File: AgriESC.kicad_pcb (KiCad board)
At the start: 2 copper layers, 80.8 x 69.6 mm, 309 parts, among them J1 SUPPLY, J10 GPIO, J11 USB_OTG, J12 HALL_ENC, J2 PH_A, J3 PH_B, J4 PH_C, J6 COMM, J7 SERVO, J8 CAN, J9 SWD, SW1 SW_SPDT, U1 FDMS7698, U10 STM32F405RGT6, U11 DRV8303, U12 TJA1051TK-3, U13 LMR16006YQ, U14 MCP1700-3302E_SOT23, U15 MCP1700-3302E_SOT23, U2 FDMS7698, U3 FDMS7698, U4 FDMS7698, U5 FDMS7698, U6 FDMS7698, U7 MAX9920, U8 MAX9920, U9 MAX9920, Y1 8M Resonator

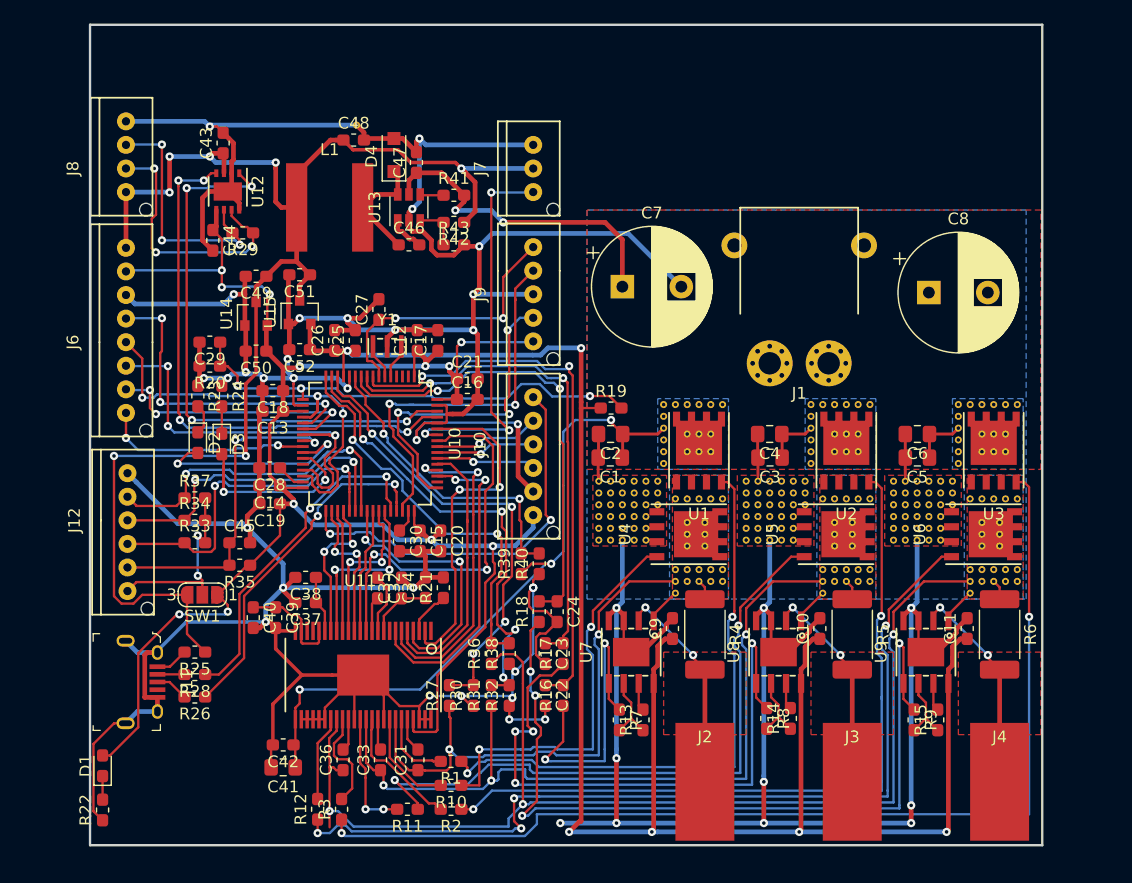
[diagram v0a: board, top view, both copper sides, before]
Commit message: Moved USB and added moutning points
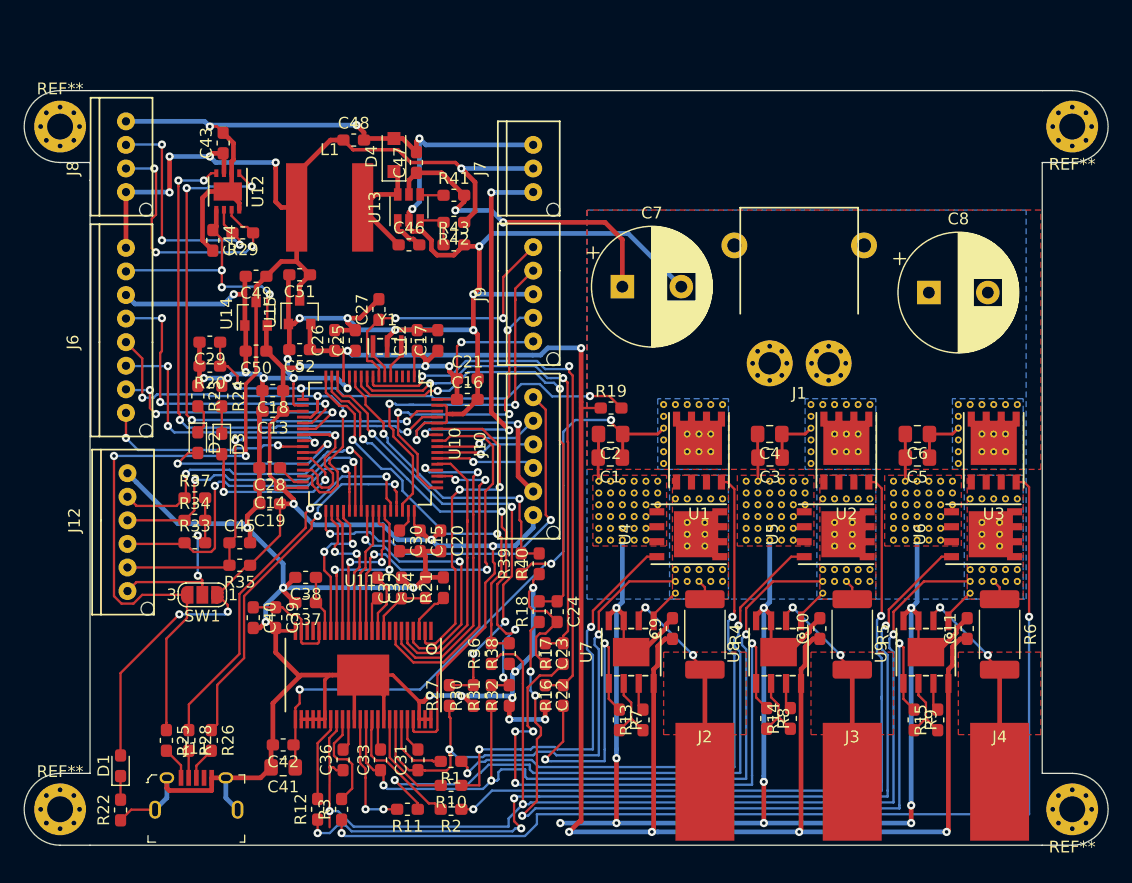
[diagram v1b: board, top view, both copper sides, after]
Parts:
- removed the REF** at (92.2, -5.21)
- added REF**: MountingHole_2.2mm_M2_Pad_Via, Mounting_Holes:MountingHole_2.2mm_M2_Pad_Via, F.Cu at (152.9, -5.08)
- added REF**: MountingHole_2.2mm_M2_Pad_Via, Mounting_Holes:MountingHole_2.2mm_M2_Pad_Via, F.Cu at (67.1, -5.08)
- added REF**: MountingHole_2.2mm_M2_Pad_Via, Mounting_Holes:MountingHole_2.2mm_M2_Pad_Via, F.Cu at (152.9, 52.8)
- added REF**: MountingHole_2.2mm_M2_Pad_Via, Mounting_Holes:MountingHole_2.2mm_M2_Pad_Via, F.Cu at (67.1, 52.8)
- moved J11 8.77 mm to (78.6, 50.2), turned to 0 degrees
- moved R25 7.87 mm to (76.1, 47.0), turned to 270 degrees
- moved R28 5.61 mm to (78.0, 47.0), turned to 270 degrees
- moved R26 3.94 mm to (79.9, 47.0), turned to 270 degrees
- moved D1 1.52 mm to (72.2, 49.1)
- moved R22 1.52 mm to (72.2, 52.9)
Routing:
- net SL_A: track 538.7 -> 526.6 mm
- net +5V: track 122.6 -> 129.3 mm
- net USB_DM: track 29.1 -> 33.7 mm
- net USB_DP: track 29.7 -> 32.3 mm
- net VCC: track 158.6 -> 157.7 mm
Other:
- board size 80.8 x 69.6 mm -> 91.9 x 64 mm

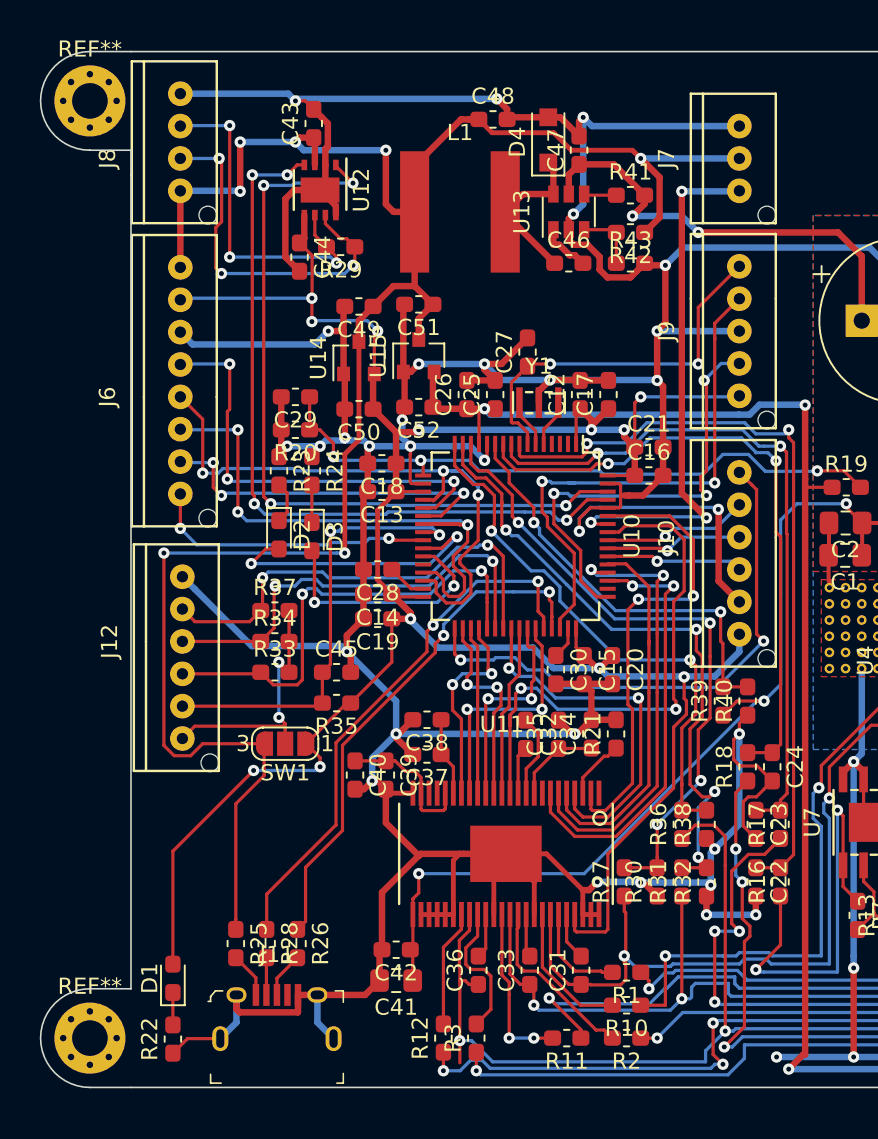
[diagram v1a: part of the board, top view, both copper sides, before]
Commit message: Added more ground planes to digital section
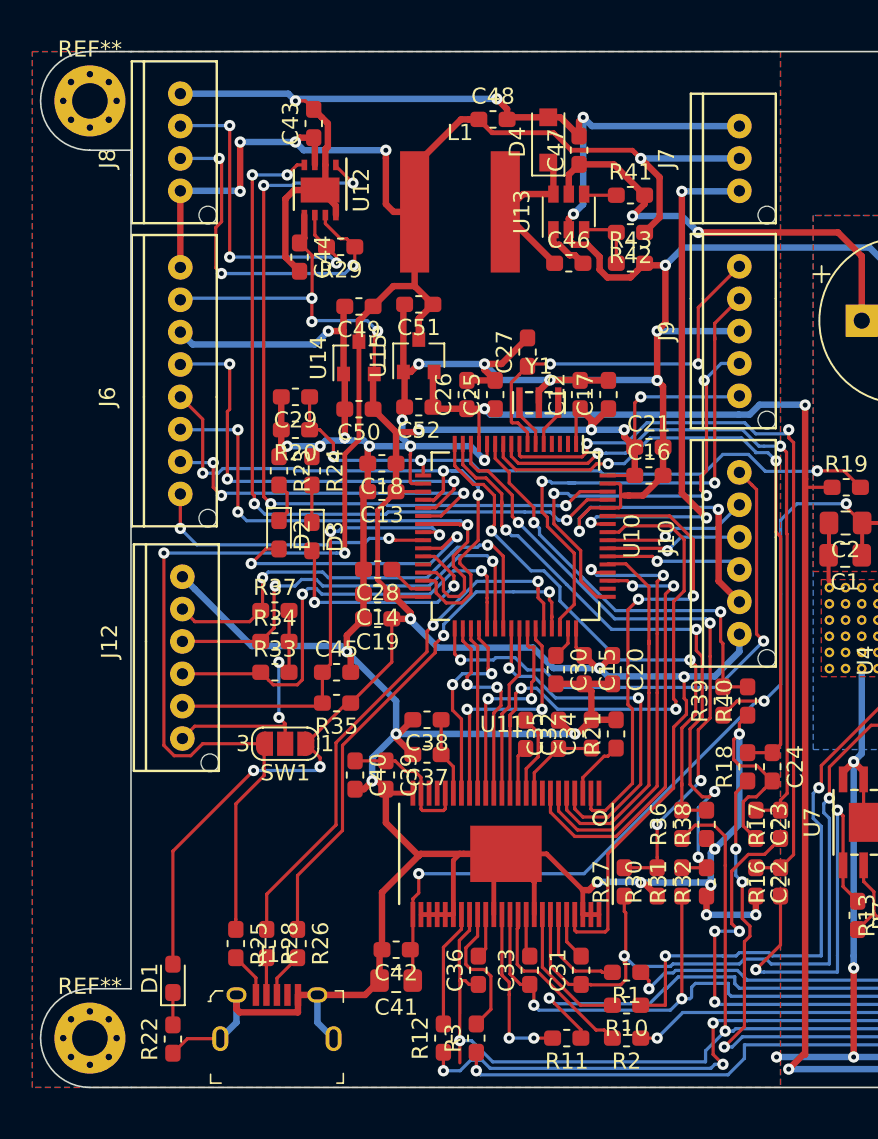
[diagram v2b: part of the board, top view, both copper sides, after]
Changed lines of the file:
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@@
   )
   (setup
-    (last_trace_width 0.4)
+    (last_trace_width 0.2)
     (user_trace_width 0.2)
     (user_trace_width 0.3)
@@
   (segment (start 88.914119 27.954119) (end 88.914119 27.275881) (width 0.2) (layer B.Cu) (net 79))
   (segment (start 90.932 25.258) (end 93.228258 25.258) (width 0.2) (layer B.Cu) (net 79))
-  (segment (start 80.382072 42.285928) (end 82.66399 40.00401) (width 0.2) (layer F.Cu) (net 79))
-  (segment (start 80.382072 45.615928) (end 80.382072 42.285928) (width 0.2) (layer F.Cu) (net 79))
-  (segment (start 79.883 46.115) (end 80.382072 45.615928) (width 0.2) (layer F.Cu) (net 79))
+  (segment (start 79.883 42.785) (end 82.66399 40.00401) (width 0.2) (layer F.Cu) (net 79))
+  (segment (start 79.883 46.115) (end 79.883 42.785) (width 0.2) (layer F.Cu) (net 79))
   (via (at 93.532791 20.97) (size 0.7) (drill 0.3) (layers F.Cu B.Cu) (net 80))
   (segment (start 93.532791 20.97) (end 97.028 24.465209) (width 0.2) (layer B.Cu) (net 80))
@@
   (segment (start 93.157365 20.594574) (end 93.157365 19.283386) (width 0.2) (layer F.Cu) (net 80))
   (segment (start 93.157365 19.283386) (end 91.653979 17.78) (width 0.2) (layer F.Cu) (net 80))
-  (segment (start 95.098 27.516) (end 95.098 26.816) (width 0.2) (layer F.Cu) (net 81) (status 10))
   (via (at 94.74855 24.608) (size 0.7) (drill 0.3) (layers F.Cu B.Cu) (net 81))
-  (segment (start 94.74855 26.46655) (end 94.74855 24.608) (width 0.2) (layer F.Cu) (net 81))
-  (segment (start 95.098 26.816) (end 94.74855 26.46655) (width 0.2) (layer F.Cu) (net 81))
   (via (at 88.264119 27.317721) (size 0.7) (drill 0.3) (layers F.Cu B.Cu) (net 81))
   (segment (start 88.264119 27.317721) (end 87.884 27.69784) (width 0.2) (layer F.Cu) (net 81))
@@
   (segment (start 77.978 43.942) (end 77.978 46.115) (width 0.2) (layer F.Cu) (net 81))
   (segment (start 82.26398 39.65602) (end 77.978 43.942) (width 0.2) (layer F.Cu) (net 81))
+  (segment (start 94.74855 25.102974) (end 94.74855 24.608) (width 0.2) (layer F.Cu) (net 81))
+  (segment (start 95.098 25.968673) (end 94.74855 25.619223) (width 0.2) (layer F.Cu) (net 81))
+  (segment (start 94.74855 25.619223) (end 94.74855 25.102974) (width 0.2) (layer F.Cu) (net 81))
+  (segment (start 95.098 27.516) (end 95.098 25.968673) (width 0.2) (layer F.Cu) (net 81))
   (segment (start 92.507365 19.683182) (end 92.507365 19.812) (width 0.2) (layer F.Cu) (net 82))
   (segment (start 92.507365 19.199085) (end 92.507365 19.812) (width 0.2) (layer F.Cu) (net 82))
@@
       )
     )
+  )
+  (zone (net 1) (net_name SL_A) (layer F.Cu) (hatch edge 0.508)
+    (connect_pads (clearance 0.5))
+    (min_thickness 0.254)
+    (fill yes (arc_segments 16) (thermal_gap 0.508) (thermal_bridge_width 0.508))
+    (polygon
+      (pts
+        (xy 63.5 -8.128) (xy 109.728 -8.128) (xy 109.728 55.88) (xy 63.5 55.88) (xy 63.5 28.956)
+      )
+    )
+  )
+  (zone (net 1) (net_name SL_A) (layer B.Cu) (hatch edge 0.508)
+    (connect_pads (clearance 0.5))
+    (min_thickness 0.254)
+    (fill yes (arc_segments 16) (thermal_gap 0.508) (thermal_bridge_width 0.508))
+    (polygon
+      (pts
+        (xy 63.5 -8.128) (xy 109.728 -8.128) (xy 109.728 55.88) (xy 63.5 55.88) (xy 63.5 28.956)
+      )
+    )

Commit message: Cleaning routing
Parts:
- removed the REF** at (152.9, -5.08)
- removed the REF** at (152.9, 52.8)
- removed the REF** at (67.1, 52.8)
- added REF**: MountingHole_2.2mm_M2_Pad_Via, Mounting_Holes:MountingHole_2.2mm_M2_Pad_Via, F.Cu at (194.9, 64.7)
- added REF**: MountingHole_2.2mm_M2_Pad_Via, Mounting_Holes:MountingHole_2.2mm_M2_Pad_Via, F.Cu at (194.9, 122.6)
- added REF**: MountingHole_2.2mm_M2_Pad_Via, Mounting_Holes:MountingHole_2.2mm_M2_Pad_Via, F.Cu at (109.1, 122.6)
- moved C1 81.4 mm to (155.7, 92.8)
- moved C10 81.4 mm to (173.5, 107.2)
- moved C11 81.4 mm to (186.0, 107.2)
- moved C12 81.4 mm to (139.3, 82.8)
- moved C13 81.4 mm to (127.1, 88.8)
- moved C14 81.4 mm to (126.8, 95.2)
- moved C15 81.4 mm to (139.6, 99.8)
- moved C16 81.4 mm to (143.6, 87.8)
- moved C17 81.4 mm to (141.1, 82.8)
- moved C18 81.4 mm to (127.1, 87.1)
- moved C19 81.4 mm to (126.8, 96.7)
- moved C2 81.4 mm to (155.8, 90.8)
- moved C20 81.4 mm to (141.3, 99.8)
- moved C21 81.4 mm to (143.6, 86.1)
- moved C22 81.4 mm to (150.2, 112.9)
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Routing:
- net +5V: track 129.3 -> 121.3 mm
- net HALL_3: track 28.5 -> 28.0 mm, vias 2 -> 3
- net HALL_2: track 27.5 -> 27.6 mm, vias 2 -> 3
- net HALL_1: vias 2 -> 3
- net TEMP_MOTOR: vias 2 -> 3

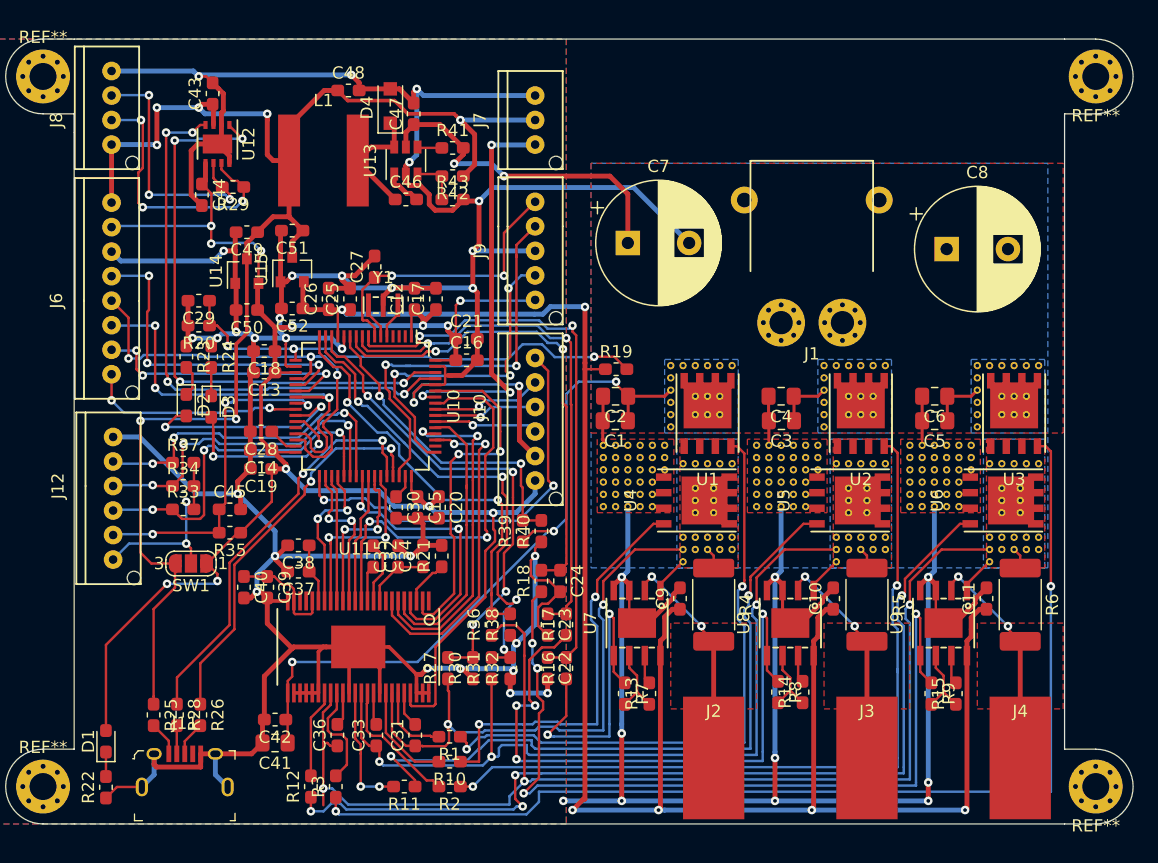
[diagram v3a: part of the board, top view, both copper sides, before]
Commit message: Rotated caps
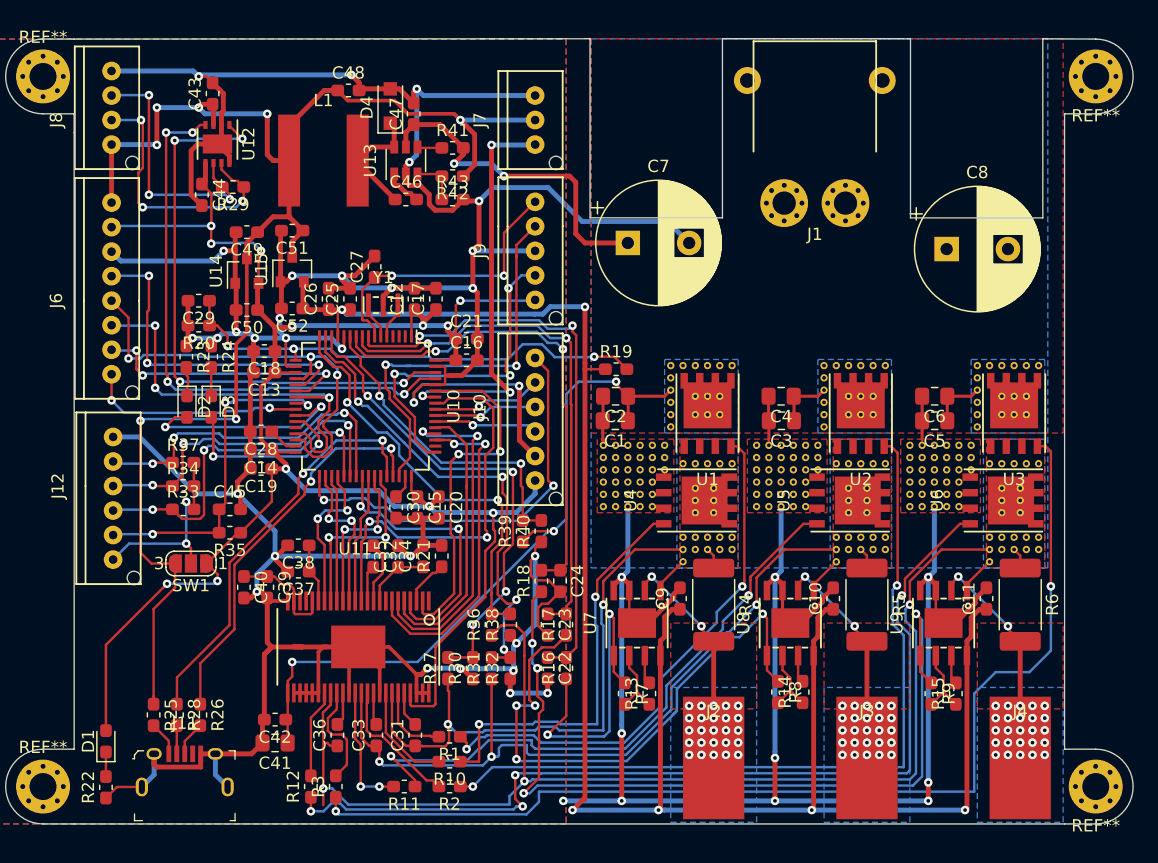
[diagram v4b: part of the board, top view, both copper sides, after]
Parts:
- moved J1 9.75 mm to (172.0, 75.0)
- moved D2 0.13 mm to (120.8, 91.6)
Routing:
- net SH_B: track 72.6 -> 66.1 mm
- net Net-(R11-Pad1): track 55.6 -> 49.2 mm
- net Net-(R1-Pad1): track 49.9 -> 43.8 mm
- net C_B: track 51.8 -> 46.2 mm
- net Net-(R3-Pad1): track 89.8 -> 87.8 mm
- net SL_A: track 526.6 -> 528.3 mm
- net Net-(J4-Pad1): track 18.3 -> 19.3 mm, vias 2 -> 27
- net Net-(J3-Pad1): track 18.7 -> 19.7 mm, vias 2 -> 27
- net Net-(R12-Pad1): track 77.4 -> 77.9 mm
- net Net-(J2-Pad1): vias 2 -> 27
- added copper zone on B.Cu, net Net-(J2-Pad1)
- added copper zone on B.Cu, net Net-(J3-Pad1)
- added copper zone on B.Cu, net Net-(J4-Pad1)
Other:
- outline, holes or cut-outs redrawn
